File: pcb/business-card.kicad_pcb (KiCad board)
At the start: 2 copper layers, 91 x 55 mm, 17 parts, among them J1 Conn_01x06, J2 Conn_01x01, J3 Conn_01x01, J4 Conn_01x01, U1 MDBT40, U2 NJM2870, Y1 Crystal

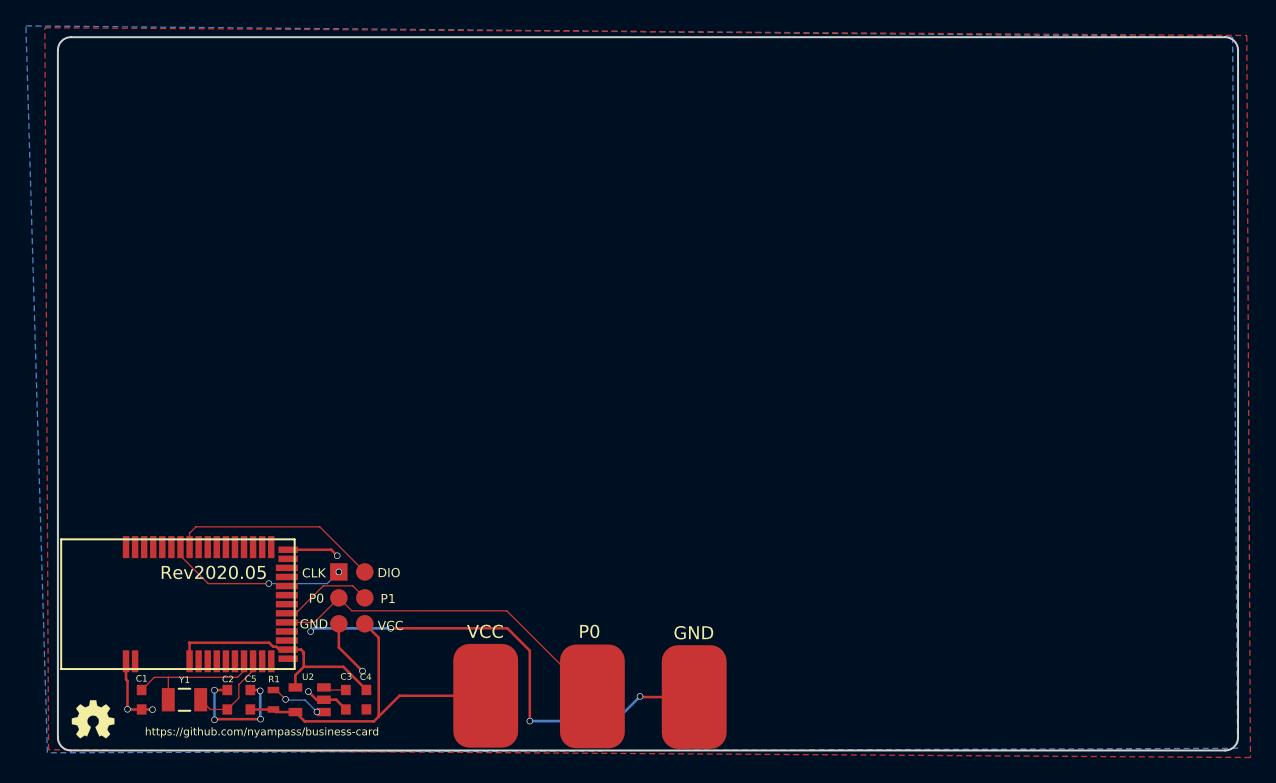
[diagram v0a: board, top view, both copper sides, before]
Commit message: Update pad style and silk info
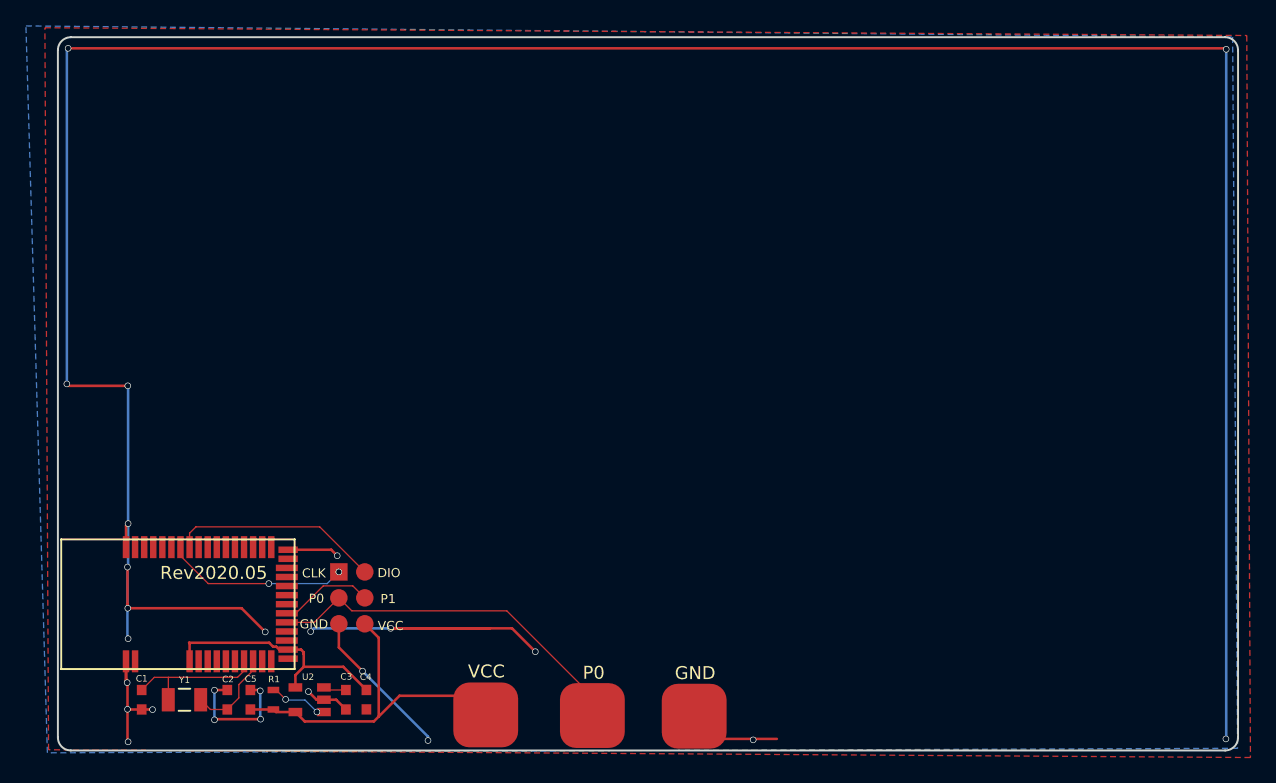
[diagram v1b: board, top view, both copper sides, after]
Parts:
- removed the G*** at (52.7, 102.6)
- moved J4 1.48 mm to (99.1, 102.4)
- moved J2 1.47 mm to (83.0, 102.3)
- moved J3 1.47 mm to (91.2, 102.3)
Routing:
- net GND: track 63.9 -> 279.4 mm, vias 13 -> 26
- net P0: track 26.9 -> 28.4 mm
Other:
- board text removed: "https://github.com/nyampass/business-card"
